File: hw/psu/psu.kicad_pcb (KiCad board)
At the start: 2 copper layers, 81 x 60 mm, 105 parts, among them J1 BATTERY, J2 CAN, J3 DEBUG, J4 SWD, J5 SDU, J6 HMI, J7 ECU, U1 INA180A1, U2 MCP2562-E-SN, U3 TS1117BCW33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

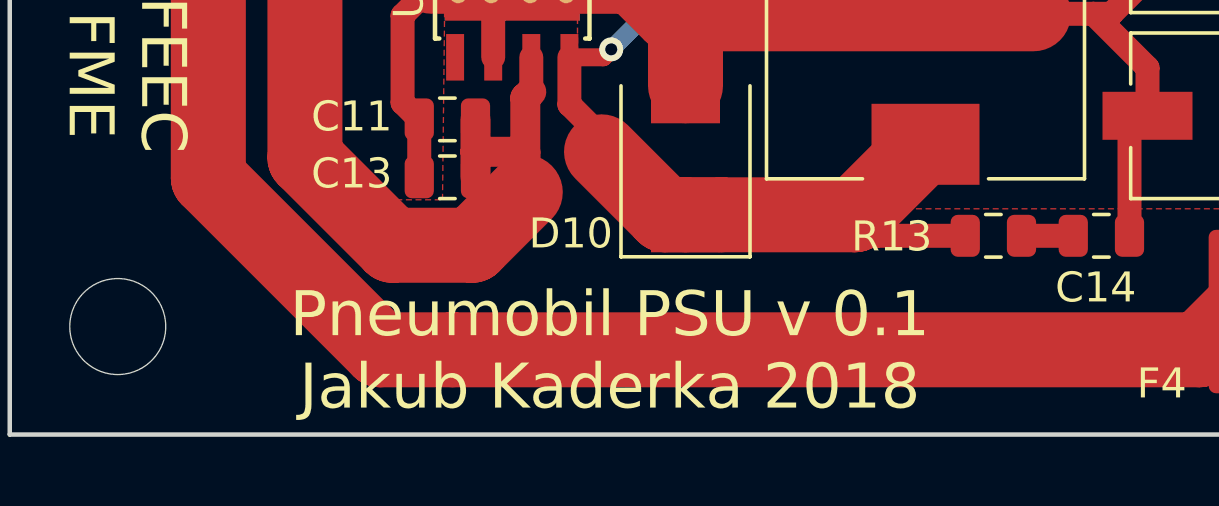
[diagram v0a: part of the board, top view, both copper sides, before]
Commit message: Added HMI and SDU boards
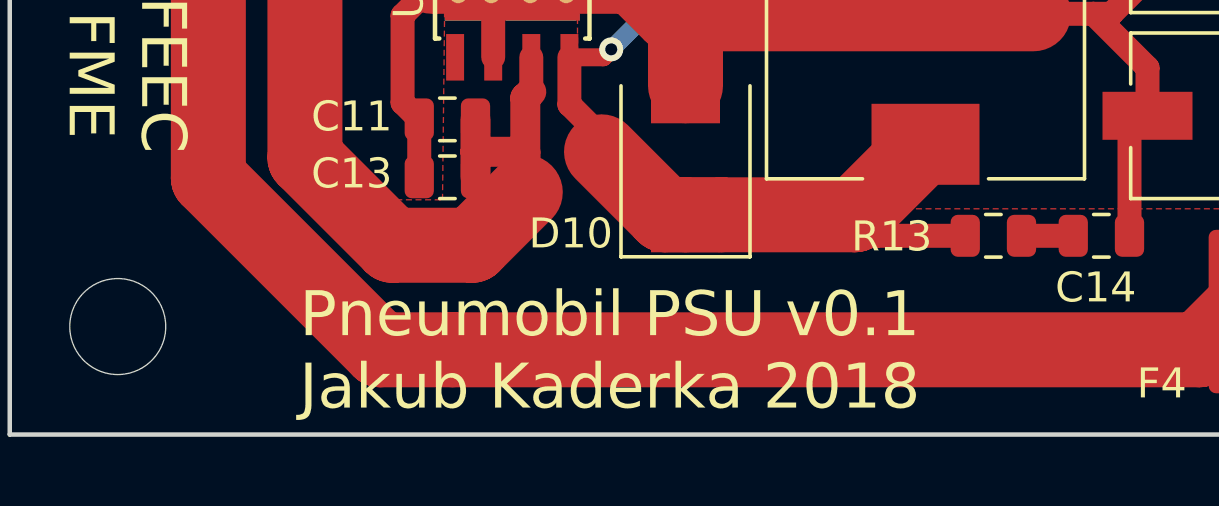
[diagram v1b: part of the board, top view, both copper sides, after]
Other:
- board text added: "Pneumobil PSU v0.1 Jakub Kaderka 2018"
- board text removed: "Pneumobil PSU v 0.1 Jakub Kaderka 2018"
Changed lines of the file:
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@@
   (title_block
     (title "BUT Pneumobil - PSU")
+    (date 2018-11-10)
     (rev 0.1)
     (company "Brno University of Technology")
@@
   )
   (setup
-    (last_trace_width 0.6)
+    (last_trace_width 0.3)
     (user_trace_width 0.25)
     (user_trace_width 0.4)
@@
     (effects (font (size 1.5 1.5) (thickness 0.3)))
   )
-  (gr_text "Pneumobil PSU v 0.1\nJakub Kaderka 2018" (at 144.5 116.2) (layer F.SilkS)
+  (gr_text "Pneumobil PSU v0.1\nJakub Kaderka 2018" (at 144.5 116.2) (layer F.SilkS)
     (effects (font (size 1.5 1.5) (thickness 0.3)))
   )

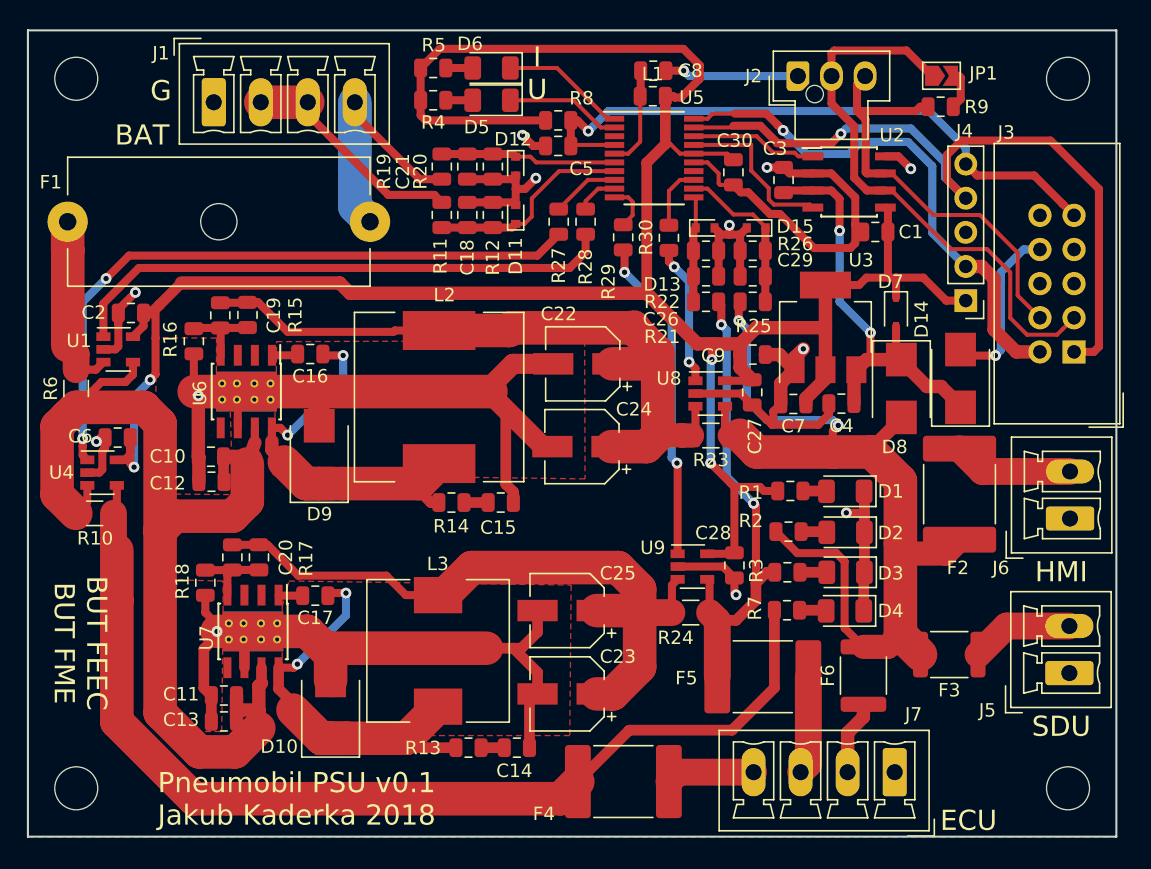
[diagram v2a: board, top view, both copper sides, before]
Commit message: Added crystal for all can equipped boards
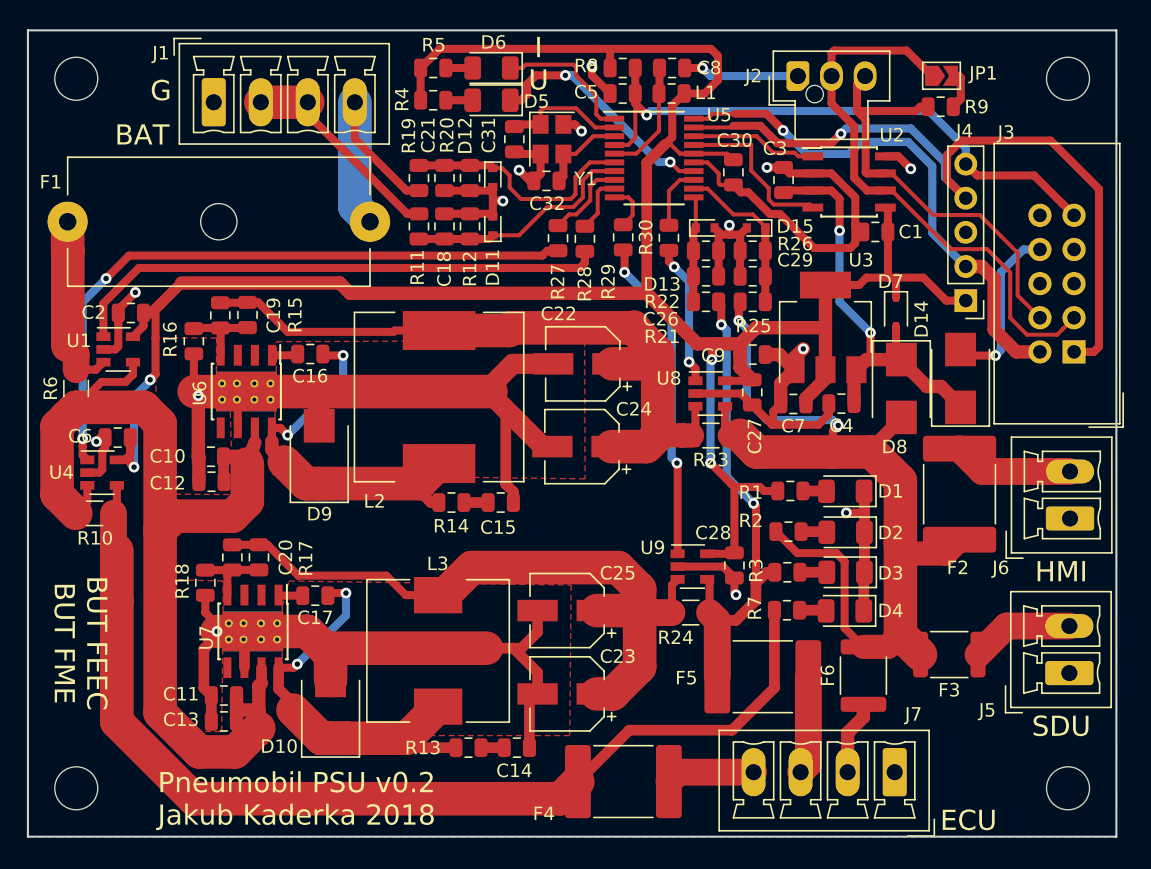
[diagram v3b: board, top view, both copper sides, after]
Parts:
- added C31: 3p9, Capacitor_SMD:C_0805_2012Metric, F.Cu at (160.7, 67.1)
- added C32: 3p9, Capacitor_SMD:C_0805_2012Metric, F.Cu at (163.1, 70.2)
- added Y1: MCSJK-7U-16.00, Crystal:Crystal_SMD_3225-4Pin_3.2x2.5mm, F.Cu at (163.5, 67.1)
- moved R8 6.18 mm to (168.8, 61.8)
- moved C5 6.18 mm to (168.8, 63.7)
- moved D12 1.90 mm to (159.1, 70.0)
- moved R11 1.90 mm to (153.6, 73.6)
- moved D11 1.90 mm to (159.1, 73.5)
- moved R19 1.90 mm to (153.6, 70.0)
- moved C18 1.90 mm to (155.5, 73.6)
- moved R12 1.90 mm to (157.4, 73.6)
- moved C21 1.90 mm to (155.5, 70.0)
- moved R20 1.90 mm to (157.4, 70.0)
- moved C8 1.41 mm to (172.4, 61.8)
- moved L1 1.41 mm to (172.4, 63.7)
- moved R28 1.28 mm to (165.9, 74.5)
- moved R27 1.23 mm to (163.9, 74.5)
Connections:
- net Net-(D6-Pad1) renamed /LED_CUR
- D5 pad 1: Net-(D5-Pad1) -> /LED_VOLT
- U5 pad 14: (no net) -> /LED_VOLT
- U5 pad 2: Net-(D5-Pad1) -> Net-(C31-Pad1)
- U5 pad 3: (no net) -> Net-(C32-Pad1)
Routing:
- net /LED_VOLT: track 0.00 -> 17.9 mm, vias 0 -> 2
- net Net-(C31-Pad1): track 0.00 -> 9.19 mm
- net Net-(D5-Pad1): track 8.59 -> 0.00 mm
- net +3V3: track 189.6 -> 182.8 mm
- net Net-(C32-Pad1): track 0.00 -> 6.48 mm
- net GND: track 227.9 -> 233.3 mm, vias 13 -> 15
- net /U_B2: track 13.1 -> 18.0 mm
- net /RESET: track 47.5 -> 44.8 mm
- net /U_B1: track 15.4 -> 17.4 mm
- net /LED_CUR: track 9.31 -> 10.7 mm
- net /BAT1: track 17.1 -> 15.7 mm
- net Net-(R28-Pad2): track 3.13 -> 4.31 mm
- net Net-(R27-Pad2): track 5.05 -> 6.23 mm
- net Net-(C8-Pad1): track 7.58 -> 8.71 mm
- net /I_BAT: track 41.3 -> 40.4 mm
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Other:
- board text added: "Pneumobil PSU v0.2 Jakub Kaderka 2018"
- board text removed: "Pneumobil PSU v0.1 Jakub Kaderka 2018"

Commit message: Fixed values of few components on psu board
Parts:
- C16, C17: value 100n -> 10n
- C19, C20: value 82p -> C
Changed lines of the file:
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@@
       (effects (font (size 1 1) (thickness 0.15)))
     )
-    (fp_text value 100n (at 0 1.65 180) (layer F.Fab)
+    (fp_text value 10n (at 0 1.65 180) (layer F.Fab)
       (effects (font (size 1 1) (thickness 0.15)))
     )
@@
       (effects (font (size 1 1) (thickness 0.15)))
     )
-    (fp_text value 100n (at 0 1.65 180) (layer F.Fab)
+    (fp_text value 10n (at 0 1.65 180) (layer F.Fab)
       (effects (font (size 1 1) (thickness 0.15)))
     )
@@
       (effects (font (size 1 1) (thickness 0.15)))
     )
-    (fp_text value 82p (at 0 1.65 270) (layer F.Fab)
+    (fp_text value C (at 0 1.65 270) (layer F.Fab)
       (effects (font (size 1 1) (thickness 0.15)))
     )
@@
       (effects (font (size 1 1) (thickness 0.15)))
     )
-    (fp_text value 82p (at 0 1.65 270) (layer F.Fab)
+    (fp_text value C (at 0 1.65 270) (layer F.Fab)
       (effects (font (size 1 1) (thickness 0.15)))
     )
